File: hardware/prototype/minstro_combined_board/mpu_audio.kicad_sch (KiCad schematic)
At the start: 21 parts, among them J501 Headset, J502 SPKR

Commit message: Combined board started layout
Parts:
- U501: footprint (none) -> BVH_Package_QFN:QFN-32-1EP_5x5mm_P0.5mm_EP2.7x2.7mm_ThermalVias
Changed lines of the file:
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@@
 			)
 		)
-		(property "Footprint" ""
+		(property "Footprint" "BVH_Package_QFN:QFN-32-1EP_5x5mm_P0.5mm_EP2.7x2.7mm_ThermalVias"
 			(at 92.71 92.71 0)
 			(effects

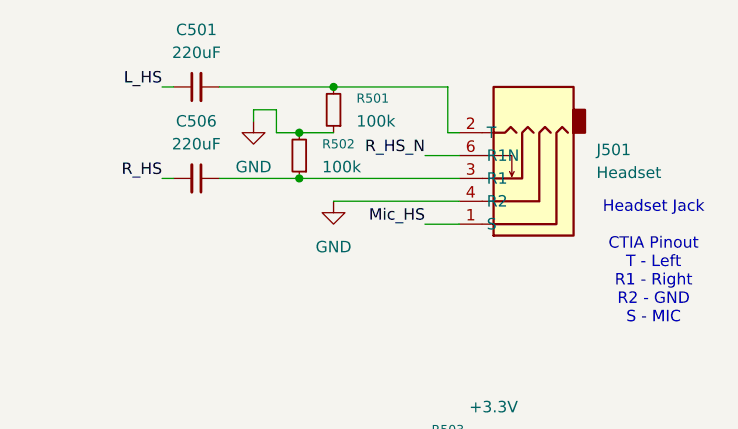
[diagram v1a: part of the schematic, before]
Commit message: Footprint assignment and PCB layout work
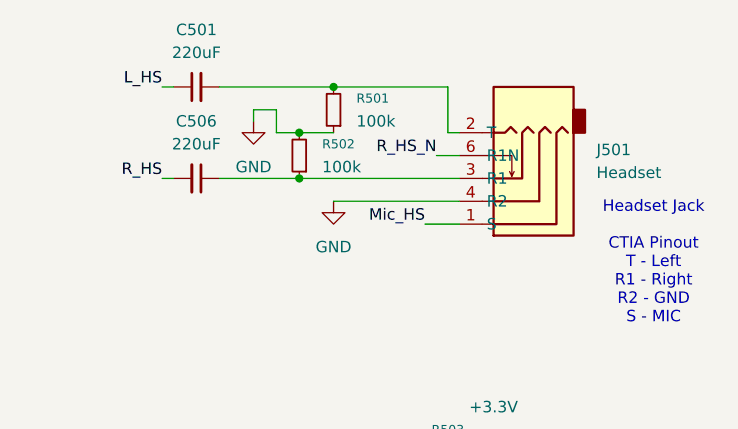
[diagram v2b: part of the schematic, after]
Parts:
- C502, C503, C504, C505, C511: footprint (none) -> Capacitor_SMD:C_0805_2012Metric
- C507, C508, C509, C510: footprint (none) -> Capacitor_SMD:C_0603_1608Metric
- FB501: footprint (none) -> BVH_Switches:TacButton_6mm_6mm
- J501: footprint (none) -> BVH_Connectors_Misc:SJ-43515RS-SMT-TR
- MK501: footprint (none) -> BVH_Audio:SameSky_CMB-6544PF_Electret_Mic_9.4d
- R501, R502, R503, R504, R505: footprint (none) -> Resistor_SMD:R_0603_1608Metric
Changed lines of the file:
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@@
 	(wire
 		(pts
-			(xy 248.92 27.94) (xy 252.73 27.94)
+			(xy 250.19 27.94) (xy 252.73 27.94)
 		)
 		(stroke
@@
 	)
 	(label "R_HS_N"
-		(at 248.92 27.94 180)
+		(at 250.19 27.94 180)
 		(effects
 			(font
@@
 			)
 		)
-		(property "Footprint" ""
+		(property "Footprint" "BVH_Switches:TacButton_6mm_6mm"
 			(at 106.68 25.908 90)
 			(effects
@@
 			)
 		)
-		(property "Footprint" ""
+		(property "Footprint" "Resistor_SMD:R_0603_1608Metric"
 			(at 234.95 27.94 0)
 			(effects
@@
 			)
 		)
-		(property "Footprint" ""
+		(property "Footprint" "Capacitor_SMD:C_0805_2012Metric"
 			(at 66.04 27.94 0)
 			(effects
@@
 			)
 		)
-		(property "Footprint" ""
+		(property "Footprint" "Capacitor_SMD:C_0603_1608Metric"
 			(at 63.5 69.85 0)
 			(effects
@@
 			)
 		)
-		(property "Footprint" ""
+		(property "Footprint" "BVH_Audio:SameSky_CMB-6544PF_Electret_Mic_9.4d"
 			(at 260.35 118.11 90)
 			(effects
@@
 			)
 		)
-		(property "Footprint" ""
+		(property "Footprint" "Capacitor_SMD:C_0805_2012Metric"
 			(at 86.36 27.94 0)
 			(effects
@@
 			)
 		)
-		(property "Footprint" ""
+		(property "Footprint" "Capacitor_SMD:C_0805_2012Metric"
 			(at 52.07 185.42 0)
 			(effects
@@
 			)
 		)
-		(property "Footprint" ""
+		(property "Footprint" "Capacitor_SMD:C_0603_1608Metric"
 			(at 50.8 81.28 0)
 			(effects
@@
 			)
 		)
-		(property "Footprint" ""
+		(property "Footprint" "Capacitor_SMD:C_0805_2012Metric"
 			(at 76.2 27.94 0)
 			(effects
@@
 			)
 		)
-		(property "Footprint" ""
+		(property "Footprint" "Resistor_SMD:R_0603_1608Metric"
 			(at 238.76 22.86 0)
 			(effects
@@
 			)
 		)
-		(property "Footprint" ""
+		(property "Footprint" "BVH_Connectors_Misc:SJ-43515RS-SMT-TR"
 			(at 259.08 30.48 0)
 			(effects
@@
 			)
 		)
-		(property "Footprint" ""
+		(property "Footprint" "Resistor_SMD:R_0603_1608Metric"
 			(at 30.48 168.91 0)
 			(effects
@@
 			)
 		)
-		(property "Footprint" ""
+		(property "Footprint" "Resistor_SMD:R_0603_1608Metric"
 			(at 251.46 63.5 0)
 			(effects
@@
 			)
 		)
-		(property "Footprint" ""
+		(property "Footprint" "Capacitor_SMD:C_0603_1608Metric"
 			(at 57.15 60.96 0)
 			(effects
@@
 			)
 		)
-		(property "Footprint" ""
+		(property "Footprint" "Capacitor_SMD:C_0805_2012Metric"
 			(at 113.03 27.94 0)
 			(effects
@@
 			)
 		)
-		(property "Footprint" ""
+		(property "Footprint" "Capacitor_SMD:C_0603_1608Metric"
 			(at 53.34 76.2 0)
 			(effects
@@
 			)
 		)
-		(property "Footprint" ""
+		(property "Footprint" "Resistor_SMD:R_0603_1608Metric"
 			(at 46.99 168.91 0)
 			(effects

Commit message: Layout WIP
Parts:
- FB501: footprint BVH_Switches:TacButton_6mm_6mm -> Resistor_SMD:R_0805_2012Metric
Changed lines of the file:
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@@
 			)
 		)
-		(property "Footprint" "BVH_Switches:TacButton_6mm_6mm"
+		(property "Footprint" "Resistor_SMD:R_0805_2012Metric"
 			(at 106.68 25.908 90)
 			(effects

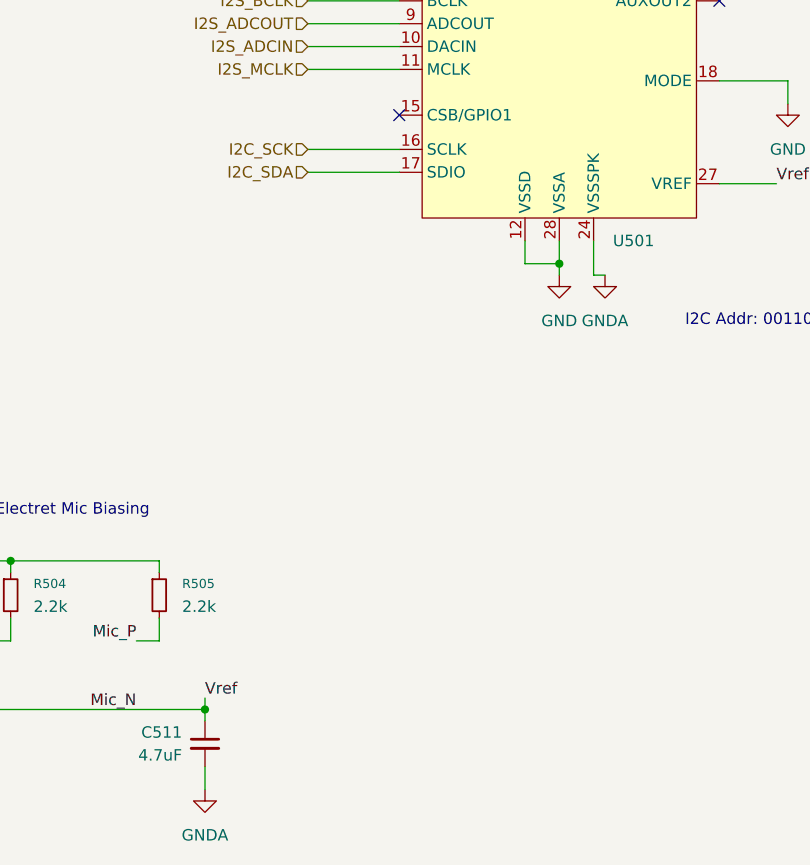
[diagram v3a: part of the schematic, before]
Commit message: Layout and routing Power and initial signals, SD card
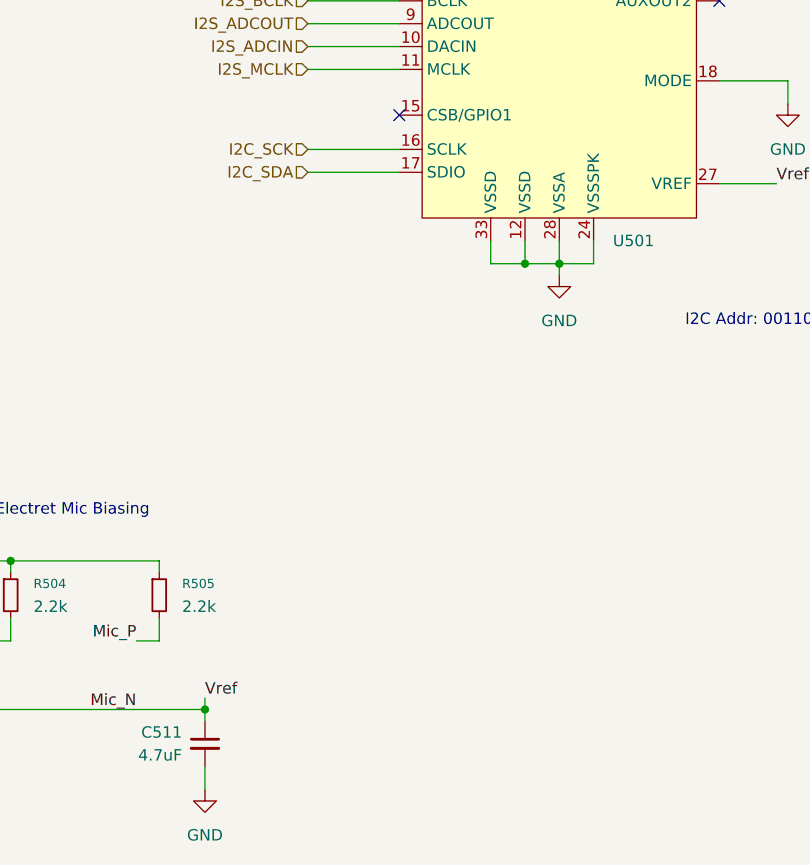
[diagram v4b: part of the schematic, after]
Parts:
- J502: footprint (none) -> Connector_JST:JST_ZH_B2B-ZR_1x02_P1.50mm_Vertical
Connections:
- net GND: now also C511.2, U501.24 (VSSSPK), U501.33 (VSSD)
- net GNDA: no longer C511.2, U501.24 (VSSSPK)
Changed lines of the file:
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@@
 	)
 	(junction
+		(at 87.63 132.08)
+		(diameter 0)
+		(color 0 0 0 0)
+	)
+	(junction
 		(at 76.2 24.13)
 		(diameter 0)
@@
 	(wire
 		(pts
+			(xy 95.25 132.08) (xy 95.25 129.54)
+		)
+		(stroke
+			(width 0)
+			(type default)
+		)
+	)
+	(wire
+		(pts
 			(xy 55.88 76.2) (xy 73.66 76.2)
 		)
@@
 	(wire
 		(pts
-			(xy 95.25 133.35) (xy 95.25 129.54)
-		)
-		(stroke
-			(width 0)
-			(type default)
-		)
-	)
-	(wire
-		(pts
 			(xy 116.84 111.76) (xy 109.22 111.76)
 		)
@@
 	(wire
 		(pts
-			(xy 96.52 133.35) (xy 95.25 133.35)
+			(xy 251.46 20.32) (xy 251.46 25.4)
 		)
 		(stroke
@@
 	(wire
 		(pts
-			(xy 251.46 20.32) (xy 251.46 25.4)
+			(xy 76.2 30.48) (xy 76.2 31.75)
 		)
 		(stroke
@@
 	(wire
 		(pts
-			(xy 76.2 30.48) (xy 76.2 31.75)
+			(xy 248.92 35.56) (xy 252.73 35.56)
 		)
 		(stroke
@@
 	(wire
 		(pts
-			(xy 248.92 35.56) (xy 252.73 35.56)
+			(xy 83.82 129.54) (xy 83.82 132.08)
 		)
 		(stroke
@@
 	(wire
 		(pts
+			(xy 83.82 132.08) (xy 87.63 132.08)
+		)
+		(stroke
+			(width 0)
+			(type default)
+		)
+	)
+	(wire
+		(pts
 			(xy 25.4 181.61) (xy 52.07 181.61)
 		)
@@
 	(wire
 		(pts
+			(xy 91.44 132.08) (xy 95.25 132.08)
+		)
+		(stroke
+			(width 0)
+			(type default)
+		)
+	)
+	(wire
+		(pts
 			(xy 234.95 25.4) (xy 238.76 25.4)
 		)
@@
 	)
 	(symbol
-		(lib_id "power:GNDA")
-		(at 96.52 133.35 0)
-		(unit 1)
-		(exclude_from_sim no)
-		(in_bom yes)
-		(on_board yes)
-		(dnp no)
-		(fields_autoplaced yes)
-		(property "Reference" "#PWR0511"
-			(at 96.52 139.7 0)
-			(effects
-				(font
-					(size 1.27 1.27)
-				)
-				(hide yes)
-			)
-		)
-		(property "Value" "GNDA"
-			(at 96.52 138.43 0)
-			(effects
-				(font
-					(size 1.27 1.27)
-				)
-			)
-		)
-		(property "Footprint" ""
-			(at 96.52 133.35 0)
-			(effects
-				(font
-					(size 1.27 1.27)
-				)
-				(hide yes)
-			)
-		)
-		(property "Datasheet" ""
-			(at 96.52 133.35 0)
-			(effects
-				(font
-					(size 1.27 1.27)
-				)
-				(hide yes)
-			)
-		)
-		(property "Description" "Power symbol creates a global label with name \"GNDA\" , analog ground"
-			(at 96.52 133.35 0)
-			(effects
-				(font
-					(size 1.27 1.27)
-				)
-				(hide yes)
-			)
-		)
-		(pin "1"
-		)
-		(instances
-			(project ""
-				(path "/abd7db12-40ec-457f-8963-ac0fca439f58/a6e0d94b-c4e5-4aef-afc1-e4ded1dc79f8"
-					(reference "#PWR0511")
-					(unit 1)
-				)
-			)
-			(project ""
-				(path "/edc2d64f-9cdb-4ab0-b2de-c3cfa55e1c10/9fd1c103-4dad-4bda-8b9e-cec55eee41ff"
-					(reference "#PWR0511")
-					(unit 1)
-				)
-			)
-		)
-	)
-	(symbol
 		(lib_id "Device:FerriteBead_Small")
 		(at 106.68 24.13 90)
@@
 			)
 		)
-		(property "Footprint" ""
+		(property "Footprint" "Connector_JST:JST_ZH_B2B-ZR_1x02_P1.50mm_Vertical"
 			(at 261.62 83.82 0)
 			(effects
@@
 	)
 	(symbol
-		(lib_id "power:GNDA")
-		(at 52.07 190.5 0)
+		(lib_id "power:GND")
+		(at 63.5 33.02 0)
 		(unit 1)
 		(exclude_from_sim no)
@@
 		(dnp no)
 		(fields_autoplaced yes)
-		(property "Reference" "#PWR0512"
-			(at 52.07 196.85 0)
+		(property "Reference" "#PWR0504"
+			(at 63.5 39.37 0)
 			(effects
 				(font
@@
 			)
 		)
-		(property "Value" "GNDA"
-			(at 52.07 195.58 0)
+		(property "Value" "GND"
+			(at 63.5 38.1 0)
 			(effects
 				(font
@@
 		)
 		(property "Footprint" ""
-			(at 52.07 190.5 0)
+			(at 63.5 33.02 0)
 			(effects
 				(font
@@
 		)
 		(property "Datasheet" ""
-			(at 52.07 190.5 0)
+			(at 63.5 33.02 0)
 			(effects
 				(font
@@
 			)
 		)
-		(property "Description" "Power symbol creates a global label with name \"GNDA\" , analog ground"
-			(at 52.07 190.5 0)
+		(property "Description" "Power symbol creates a global label with name \"GND\" , ground"
+			(at 63.5 33.02 0)
 			(effects
 				(font
@@
 			(project "display_board"
 				(path "/abd7db12-40ec-457f-8963-ac0fca439f58/a6e0d94b-c4e5-4aef-afc1-e4ded1dc79f8"
-					(reference "#PWR0512")
+					(reference "#PWR0504")
 					(unit 1)
 				)
@@
 			(project "display_board"
 				(path "/edc2d64f-9cdb-4ab0-b2de-c3cfa55e1c10/9fd1c103-4dad-4bda-8b9e-cec55eee41ff"
-					(reference "#PWR0512")
+					(reference "#PWR0504")
 					(unit 1)
 				)
@@
 	(symbol
 		(lib_id "power:GND")
-		(at 63.5 33.02 0)
+		(at 52.07 190.5 0)
 		(unit 1)
 		(exclude_from_sim no)
@@
 		(dnp no)
 		(fields_autoplaced yes)
-		(property "Reference" "#PWR0504"
-			(at 63.5 39.37 0)
+		(property "Reference" "#PWR0511"
+			(at 52.07 196.85 0)
 			(effects
 				(font
@@
 		)
 		(property "Value" "GND"
-			(at 63.5 38.1 0)
+			(at 52.07 195.58 0)
 			(effects
 				(font
@@
 		)
 		(property "Footprint" ""
-			(at 63.5 33.02 0)
+			(at 52.07 190.5 0)
 			(effects
 				(font
@@
 		)
 		(property "Datasheet" ""
-			(at 63.5 33.02 0)
+			(at 52.07 190.5 0)
 			(effects
 				(font
@@
 		)
 		(property "Description" "Power symbol creates a global label with name \"GND\" , ground"
-			(at 63.5 33.02 0)
+			(at 52.07 190.5 0)
 			(effects
 				(font
@@
 		)
 		(instances
-			(project "display_board"
-				(path "/abd7db12-40ec-457f-8963-ac0fca439f58/a6e0d94b-c4e5-4aef-afc1-e4ded1dc79f8"
-					(reference "#PWR0504")
-					(unit 1)
-				)
-			)
-			(project "display_board"
+			(project "minstro_combined_board"
 				(path "/edc2d64f-9cdb-4ab0-b2de-c3cfa55e1c10/9fd1c103-4dad-4bda-8b9e-cec55eee41ff"
-					(reference "#PWR0504")
+					(reference "#PWR0511")
 					(unit 1)
 				)
@@
 		(pin "31"
 		)
+		(pin "33"
+		)
 		(instances

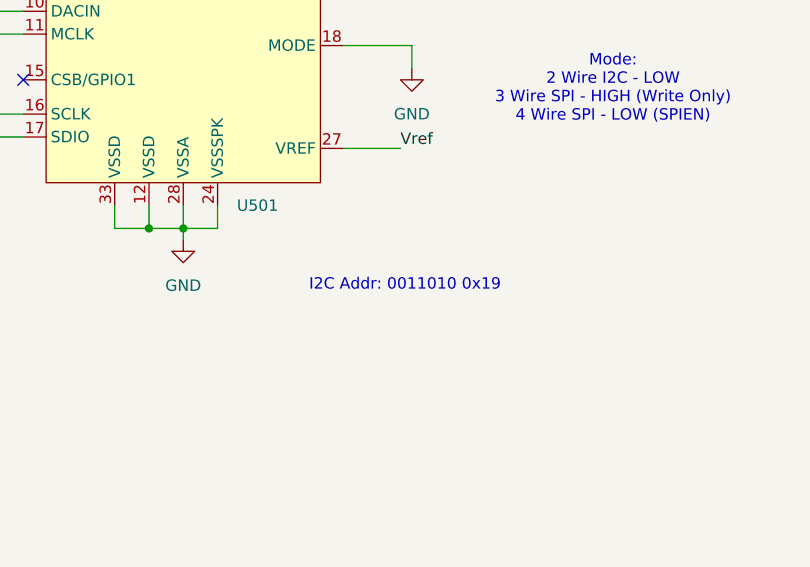
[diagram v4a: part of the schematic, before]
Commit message: Bringup WIP.  I2C enumerating.
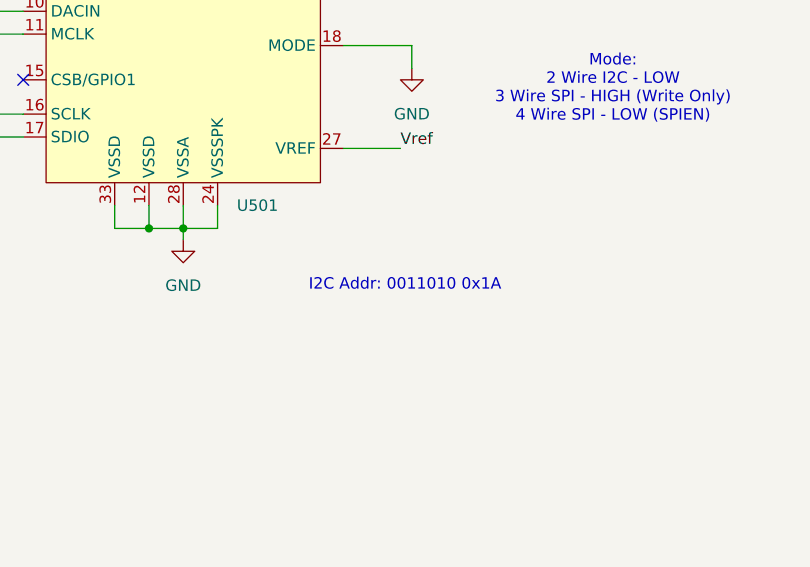
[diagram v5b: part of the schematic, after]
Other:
- note added: "I2C Addr: 0011010 0x1A"
- note removed: "I2C Addr: 0011010 0x19"
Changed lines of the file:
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@@
 		)
 	)
-	(text "I2C Addr: 0011010 0x19"
+	(text "I2C Addr: 0011010 0x1A"
 		(exclude_from_sim no)
 		(at 116.078 138.43 0)
